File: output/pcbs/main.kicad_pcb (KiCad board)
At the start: 2 copper layers, 104.3 x 89 mm, 113 parts, among them SW1 CPG1316S01D02_reversible_mike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, SW10 CPG1316S01D02_reversible_mike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, SW11 CPG1316S01D02_reversible_mike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, SW12 CPG1316S01D02_reversible_mike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, SW13 CPG1316S01D02_reversible_mike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, SW14 CPG1316S01D02_reversible_mike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, SW15 CPG1316S01D02_reversible_mike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, SW16 CPG1316S01D02_reversible_mike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, SW17 CPG1316S01D02_reversible_mike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, SW18 CPG1316S01D02_reversible_mike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, SW2 CPG1316S01D02_reversible_mike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, SW3 CPG1316S01D02_reversible_mike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, SW4 CPG1316S01D02_reversible_mike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, SW5 CPG1316S01D02_reversible_mike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, SW6 CPG1316S01D02_reversible_mike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, SW7 CPG1316S01D02_reversible_mike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, SW8 CPG1316S01D02_reversible_mike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, SW9 CPG1316S01D02_reversible_mike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

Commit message: Close the design gaps: coin cell, per-key LEDs, ZMK dongle, JLC files, case
- Reversible footprints (2-pin SMD, SOT-23, slide switch, CR2032 holder,
  M2 holes) that mirror their B-side copper, so one PCB assembles as the
  left half on top and the right half on the bottom.
- Coin cell power path (CR2032 -> switch -> B5819W -> XIAO BAT+), per-key
  0603 LEDs with one PWM-dimmed low-side MOSFET.
- Routed board via Freerouting plus a finisher for nets it misreads, GND
  pours, DRC with no unconnected items, gerbers, BOM and CPL for both sides.
- ZMK v0.3 config: dongle central, two peripheral halves, backlight off by
  default at 10% with idle auto-off; GitHub Actions build.
- OpenSCAD uniboard case generated from the board outline.
- Old hand-routed LiPo board moved to archive/v1-lipo.

Co-Authored-By: Claude Opus 5.5 (1M context) <noreply@anthropic.com>
Claude-Session: https://claude.ai/code/session_01FPyenVXHBDq22rK9XranC3
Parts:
- removed REF** (x72): VIA-0.6mm, VIA-0.6mm
- removed T2: , E73:SPDT_C128955
- removed _73: , Connector_JST:JST_PH_S2B-PH-K_1x02_P2.00mm_Horizontal
- added BT1: CR2032, ucw:REV_CR2032_BC2003, F.Cu at (22.0, 10.0)
- added C1: 22uF, ucw:REV_0805, F.Cu at (29.0, -5.50)
- added C2: 22uF, ucw:REV_0805, F.Cu at (33.0, -3.00)
- added D19: B5819W, ucw:REV_SOD123, F.Cu at (29.0, -9.00)
- added H1: M2, ucw:M2_NPTH, F.Cu at (24.5, -59.5)
- added H2: M2, ucw:M2_NPTH, F.Cu at (2.00, 10.8)
- added H3: M2, ucw:M2_NPTH, F.Cu at (73.0, 3.00)
- added L1: LED_red_0603, ucw:REV_LED0603, F.Cu at (0.00, -2.50)
- added L10: LED_red_0603, ucw:REV_LED0603, F.Cu at (51.0, -14.4)
- added L11: LED_red_0603, ucw:REV_LED0603, F.Cu at (51.0, -31.4)
- added L12: LED_red_0603, ucw:REV_LED0603, F.Cu at (51.0, -48.4)
- added L13: LED_red_0603, ucw:REV_LED0603, F.Cu at (68.0, -11.0)
- added L14: LED_red_0603, ucw:REV_LED0603, F.Cu at (68.0, -28.0)
- added L15: LED_red_0603, ucw:REV_LED0603, F.Cu at (68.0, -45.0)
- added L16: LED_red_0603, ucw:REV_LED0603, F.Cu at (44.2, 6.00)
- added L17: LED_red_0603, ucw:REV_LED0603, F.Cu at (63.9, 8.14)
- added L18: LED_red_0603, ucw:REV_LED0603, F.Cu at (84.3, 14.4)
- added L2: LED_red_0603, ucw:REV_LED0603, F.Cu at (0.00, -19.5)
- added L3: LED_red_0603, ucw:REV_LED0603, F.Cu at (0.00, -36.5)
- added L4: LED_red_0603, ucw:REV_LED0603, F.Cu at (17.0, -16.1)
- added L5: LED_red_0603, ucw:REV_LED0603, F.Cu at (17.0, -33.1)
- added L6: LED_red_0603, ucw:REV_LED0603, F.Cu at (17.0, -50.1)
- added L7: LED_red_0603, ucw:REV_LED0603, F.Cu at (34.0, -22.9)
- added L8: LED_red_0603, ucw:REV_LED0603, F.Cu at (34.0, -39.9)
- added L9: LED_red_0603, ucw:REV_LED0603, F.Cu at (34.0, -56.9)
- added Q1: AO3400A, ucw:REV_SOT-23, F.Cu at (39.0, -7.00)
- added R1: 1k, ucw:REV_0603, F.Cu at (-2.60, 7.20)
- added R10: 1k, ucw:REV_0603, F.Cu at (48.4, -4.70)
- added R11: 1k, ucw:REV_0603, F.Cu at (48.4, -21.7)
- added R12: 1k, ucw:REV_0603, F.Cu at (48.4, -38.7)
- added R13: 1k, ucw:REV_0603, F.Cu at (65.4, -1.30)
- added R14: 1k, ucw:REV_0603, F.Cu at (65.4, -18.3)
- added R15: 1k, ucw:REV_0603, F.Cu at (65.4, -35.3)
- added R16: 1k, ucw:REV_0603, F.Cu at (40.3, 1.30)
- added R17: 1k, ucw:REV_0603, F.Cu at (61.4, 2.59)
- added R18: 1k, ucw:REV_0603, F.Cu at (83.8, 8.29)
- added R19: 100k, ucw:REV_0603, F.Cu at (39.0, -2.50)
- added R2: 1k, ucw:REV_0603, F.Cu at (-2.60, -9.80)
- added R3: 1k, ucw:REV_0603, F.Cu at (-2.60, -26.8)
- added R4: 1k, ucw:REV_0603, F.Cu at (14.4, -6.40)
- added R5: 1k, ucw:REV_0603, F.Cu at (14.4, -23.4)
- added R6: 1k, ucw:REV_0603, F.Cu at (14.4, -40.4)
- added R7: 1k, ucw:REV_0603, F.Cu at (31.4, -13.2)
- added R8: 1k, ucw:REV_0603, F.Cu at (31.4, -30.2)
- added R9: 1k, ucw:REV_0603, F.Cu at (31.4, -47.2)
- D1, D10, D11, D12, D13, D14, D15, D16, D17, D18, D2, D3, D4, D5, D6, D7, D8, D9: value (none) -> 1N4148W; footprint PCM_Diode_SMD_Handsoldering_AKL:D_SOD-123 -> ucw:REV_SOD123
- SW1, SW10, SW11, SW12, SW13, SW14, SW15, SW16, SW17, SW18, SW2, SW3, SW4, SW5, SW6, SW7, SW8, SW9: value CPG1316S01D02_reversible_mikefives -> CPG1316S01D02_reversible; footprint leptiosis:CPG1316S01D02_reversible_mikefives -> CPG1316S01D02_reversible
- T1: footprint E73:SPDT_C128955 -> ucw:REV_SPDT_C128955
- moved D16 283.0 mm to (45.5, 1.30)
- moved D17 279.7 mm to (66.4, 3.94), turned to -15 degrees
- moved PAD1 275.5 mm to (0.00, -42.5)
- moved SW1 275.5 mm to (0.00, 0.00)
- moved SW10 275.5 mm to (51.0, -11.9)
- moved SW11 275.5 mm to (51.0, -28.9)
- moved SW12 275.5 mm to (51.0, -45.9)
- moved SW13 275.5 mm to (68.0, -8.50)
- moved SW14 275.5 mm to (68.0, -25.5)
- moved SW15 275.5 mm to (68.0, -42.5)
- moved SW16 275.5 mm to (44.2, 8.50)
- moved SW2 275.5 mm to (0.00, -17.0)
- moved SW3 275.5 mm to (0.00, -34.0)
- moved SW4 275.5 mm to (17.0, -13.6)
- moved SW5 275.5 mm to (17.0, -30.6)
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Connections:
- T1 pad 1: BAT+ -> BAT
- T1 pad 2: RAW -> SW_BAT
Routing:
- net P4: track 212.1 -> 0.00 mm
- net P10: track 168.8 -> 0.00 mm
- net P0: track 155.8 -> 0.00 mm
- net P9: track 146.5 -> 0.00 mm
- net BAT+: track 141.1 -> 0.00 mm, vias 1 -> 0
- net P1: track 130.0 -> 0.00 mm
- net P2: track 116.6 -> 0.00 mm
- net P8: track 110.5 -> 0.00 mm
- net GND: track 99.0 -> 0.00 mm
- net P3: track 63.8 -> 0.00 mm
- net P5: track 60.4 -> 0.00 mm
- net ring_home: track 54.3 -> 0.00 mm
- net RAW: track 29.2 -> 0.00 mm
- net pinky_home: track 17.5 -> 0.00 mm
- net ring_bottom: track 12.5 -> 0.00 mm
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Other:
- board size 104.3 x 89 mm -> 103.7 x 91.1 mm
- net class Default added: clearance 0.2, trace_width 0.25, via_dia 0.8, via_drill 0.4

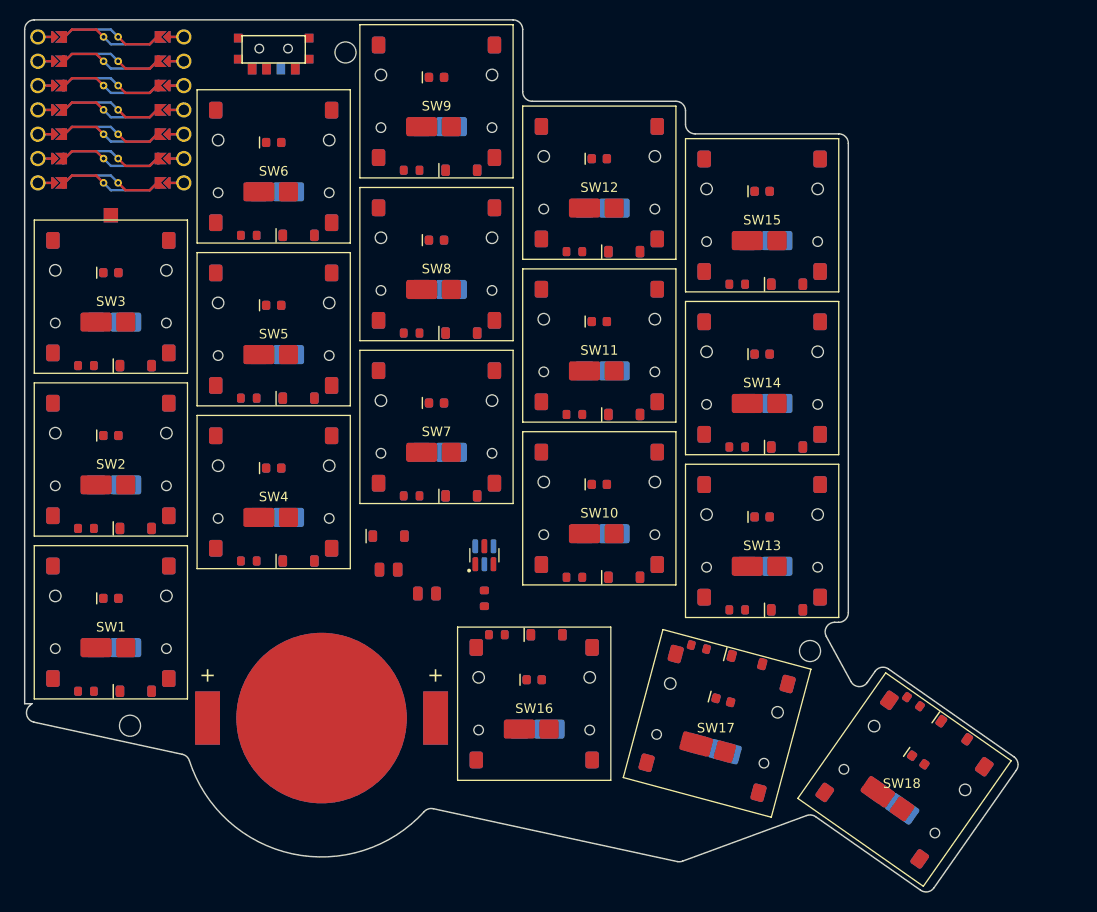
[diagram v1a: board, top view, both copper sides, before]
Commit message: Match the Chocofi key spacing, stagger and thumb cluster
Key centres now come straight from the Chocofi PCB (pashutk/chocofi):
18 x 17 mm pitch, column stagger 12 / 6 / -6.625 / -2.375 mm, thumbs at
fixed offsets from the bottom pinky key with a 0 / -15 / -30 degree fan.

The board top edge and power switch are now set from the pinky key so the
XIAO's top pin row stays on the board, and the thumb M2 hole moved off the
middle thumb diode. finish_routes.py reroutes tracks Freerouting leaves
inside the 0.3 mm edge rule, and the pour ties the XIAO's via-like GND
pads in solidly. Board rerouted, DRC has no new errors, gerbers, CPL and
case regenerated.

Co-Authored-By: Claude Opus 5.5 (1M context) <noreply@anthropic.com>
Claude-Session: https://claude.ai/code/session_01EJCFFVGKLmNFccuN3tJpCU
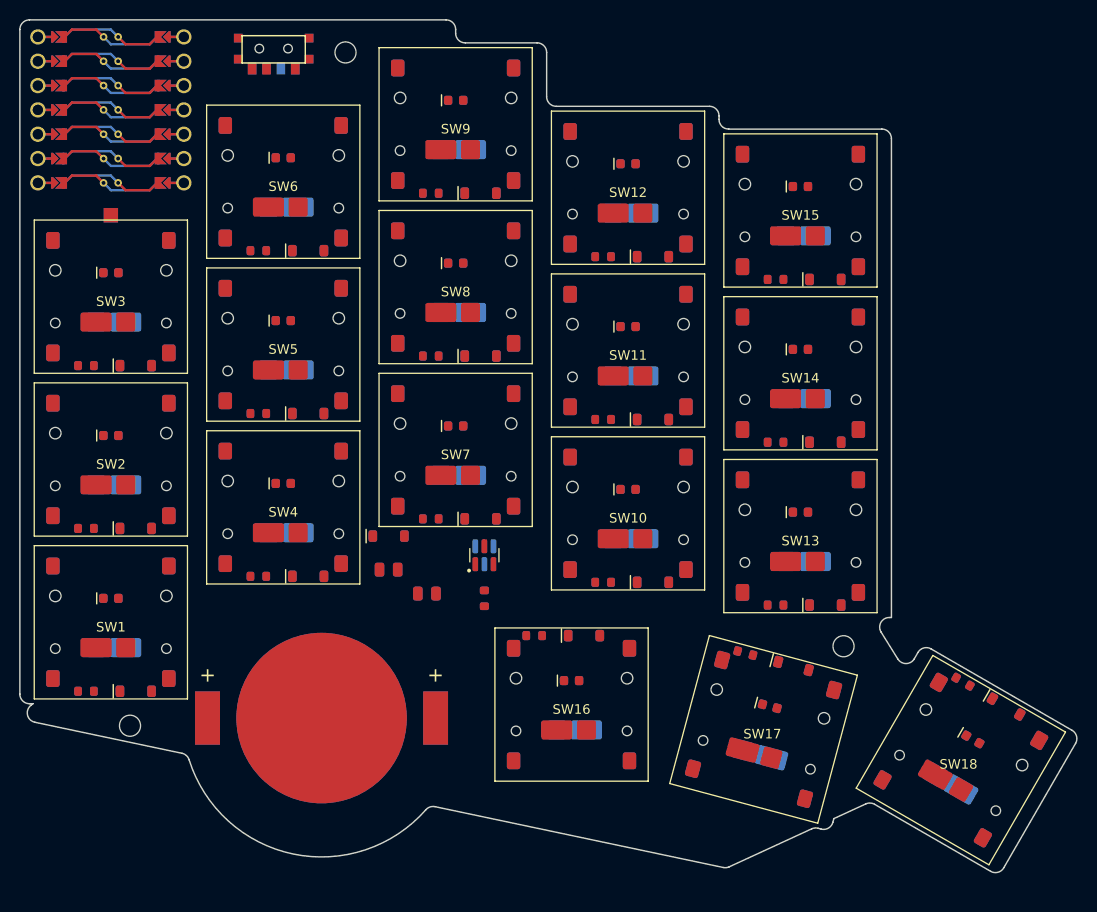
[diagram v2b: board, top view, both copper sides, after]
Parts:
- moved SW18 6.22 mm to (88.8, 14.4), turned to -30 degrees
- moved L18 6.09 mm to (90.0, 12.2), turned to -30 degrees
- moved D18 5.95 mm to (93.5, 8.80), turned to -30 degrees
- moved R18 5.57 mm to (89.0, 6.20), turned to -30 degrees
- moved R17 4.89 mm to (66.2, 3.22)
- moved SW17 4.89 mm to (68.2, 11.2)
- moved D17 4.89 mm to (71.3, 4.56)
- moved L17 4.89 mm to (68.8, 8.77)
- moved D13 4.03 mm to (74.6, -1.80)
- moved D14 4.03 mm to (74.6, -18.8)
- moved D15 4.03 mm to (74.6, -35.8)
- moved L13 4.03 mm to (72.0, -11.5)
- moved L14 4.03 mm to (72.0, -28.5)
- moved L15 4.03 mm to (72.0, -45.5)
- moved R13 4.03 mm to (69.4, -1.80)
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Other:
- board size 103.7 x 91.1 mm -> 110.4 x 89 mm
